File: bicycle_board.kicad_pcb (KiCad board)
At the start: 2 copper layers, 41.4 x 84.9 mm, 130 parts, among them J1 Micro_SD_Card, J10 USB_A, J12 Conn_01x04, J13 Conn_01x04, J2 USB_C_Receptacle_USB2.0_16P, J3 Conn_01x02, J4 Conn_01x02, J6 Conn_01x08, J7 Conn_01x05, J8 Conn_01x02, J9 Conn_01x06, Q1 Q_NMOS_GSD, Q2 Q_NMOS_GSD, Q3 Q_NMOS_GSD, Q4 Q_NMOS_GSD, Q5 Q_NMOS_GSD, Q6 Si2302, Q7 Si2302, Q8 Q_PMOS_GSD, U1 TP4056, U10 MCP603-xCH, U11 BMP280, U12 MMC5633NJL, U13 NS4168, U14 ESP32-C3-WROOM-02U, U15 CH32V203C8T6, U16 PS7516, U17 TXB0108PW, U2 SGM2039, U3 IIM-42652, U4 QMI8610, U5 AHT20, U6 SGM2033-1.8, U7 74HC595, U8 74HC595, U9 PCA9306DC1, Y1 12MHz, Y2 32.768kHz

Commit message: 连接大多数布线，做一些调整，添加覆铜
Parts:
- added C48: 100n, Capacitor_SMD:C_0402_1005Metric, B.Cu at (131.8, 106.5)
- J12: moved to F.Cu
- moved R26 16.2 mm to (133.9, 126.9), turned to -90 degrees
- moved R25 15.5 mm to (132.9, 126.9), turned to -90 degrees
- moved U9 11.5 mm to (132.5, 130.2), turned to 90 degrees
- moved R24 10.4 mm to (134.0, 133.4), turned to 90 degrees
- moved C18 9.34 mm to (130.7, 130.6), turned to 90 degrees
- moved R23 9.18 mm to (133.0, 133.4), turned to 90 degrees
- moved C11 8.68 mm to (118.2, 130.6)
- moved U4 8.68 mm to (120.5, 130.6)
- moved U3 8.68 mm to (124.8, 130.3)
- moved C10 8.68 mm to (124.0, 132.5)
- moved C12 8.68 mm to (121.0, 132.3)
- moved C33 8.68 mm to (127.5, 132.0)
- moved C9 8.68 mm to (125.8, 132.5)
- moved C17 7.51 mm to (131.5, 133.2), turned to 0 degrees
- moved C19 2.52 mm to (130.7, 138.5), turned to 0 degrees
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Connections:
- J12 pad 1: unconnected-(J12-Pin_1-Pad1) -> +3.3V
- J12 pad 2: /SCL2 -> GND
- J12 pad 3: /SDA2 -> /SCL2
- J12 pad 4: unconnected-(J12-Pin_4-Pad4) -> /SDA2
- U11 pad 2: /sensors/SPISen_CS_BMP_1V8 -> +1V8
- U11 pad 3: /sensors/SPISen_MOSI_1V8 -> /sensors/SDA1V8
- U11 pad 4: /sensors/SPISen_SCLK_1V8 -> /sensors/SCL1V8
- U11 pad 5: /sensors/SPISen_MISO_1V8 -> unconnected-(U11-SDO-Pad5)
- U13 pad 4: /I2SO_SDATA -> /I2SO_SD
- U14 pad 10: /I2SO_SD -> unconnected-(U14-IO10-Pad10)
- U14 pad 15: /I2SI_SD -> unconnected-(U14-IO3-Pad15)
- U14 pad 3: /I2SI_BCK -> unconnected-(U14-IO4-Pad3)
- U14 pad 4: /I2SI_WS -> /I2SO_SD
- U14 pad 7: /I2SO_WS -> /I2SO_BCK
- U14 pad 8: /I2SO_BCK -> /I2SO_WS
- U15 pad 16: unconnected-(U15-PA6-Pad16) -> /ADC_Isolar
- U15 pad 17: unconnected-(U15-PA7-Pad17) -> /ADC_Vbat
- U15 pad 18: unconnected-(U15-PB0-Pad18) -> /ADC_Vsolar
- U15 pad 21: /TXD -> /SCL2
- U15 pad 22: unconnected-(U15-PB11-Pad22) -> /SDA2
- U15 pad 26: unconnected-(U15-PB13-Pad26) -> /SPI_SCLK
- U15 pad 27: unconnected-(U15-PB14-Pad27) -> /SPI_MISO
- U15 pad 28: unconnected-(U15-PB15-Pad28) -> /SPI_MOSI
- U15 pad 30: unconnected-(U15-PA9-Pad30) -> /TXD
- U15 pad 31: unconnected-(U15-PA10-Pad31) -> /RXD
- U15 pad 32: unconnected-(U15-PA11-Pad32) -> /USB_CH32FS_D-
- U15 pad 33: unconnected-(U15-PA12-Pad33) -> /USB_CH32FS_D+
- U15 pad 38: unconnected-(U15-PA15-Pad38) -> /SPISen_CS_QMI_3V3
- U15 pad 39: unconnected-(U15-PB3-Pad39) -> /SPISen_SCLK_3V3
- U15 pad 40: unconnected-(U15-PB4-Pad40) -> /SPISen_MISO_3V3
- U15 pad 41: unconnected-(U15-PB5-Pad41) -> /SPISen_MOSI_3V3
- U15 pad 42: /USB_CH32FS_D- -> /SPISen_CS_TDK_3V3
- U15 pad 43: /USB_CH32FS_D+ -> /TDK_INT2_3V3
- U15 pad 45: unconnected-(U15-PB8-Pad45) -> /SCL1
- U15 pad 46: /RXD -> /SDA1
- U15 pad 7: unconnected-(U15-NRST-Pad7) -> Net-(U15-NRST)
- U17 pad 1: /sensors/SPISen_CS_QMI_1V8 -> unconnected-(U17-A1-Pad1)
- U17 pad 12: unconnected-(U17-B8-Pad12) -> /TDK_INT2_3V3
- U17 pad 13: /sensors/TDK_INT2_3V3 -> /SPISen_CS_TDK_3V3
- U17 pad 14: /sensors/SPISen_MISO_3V3 -> /SPISen_MOSI_3V3
- U17 pad 15: /sensors/SPISen_SCLK_3V3 -> /SPISen_MISO_3V3
- U17 pad 16: /sensors/SPISen_MOSI_3V3 -> /SPISen_SCLK_3V3
- U17 pad 17: /sensors/SPISen_CS_BMP_3V3 -> /SPISen_CS_QMI_3V3
- U17 pad 18: /sensors/SPISen_CS_TDK_3V3 -> unconnected-(U17-B2-Pad18)
- U17 pad 20: /sensors/SPISen_CS_QMI_3V3 -> unconnected-(U17-B1-Pad20)
- U17 pad 3: /sensors/SPISen_CS_TDK_1V8 -> unconnected-(U17-A2-Pad3)
- U17 pad 4: /sensors/SPISen_CS_BMP_1V8 -> /sensors/SPISen_CS_QMI_1V8
- U17 pad 5: /sensors/SPISen_MOSI_1V8 -> /sensors/SPISen_SCLK_1V8
- U17 pad 6: /sensors/SPISen_SCLK_1V8 -> /sensors/SPISen_MISO_1V8
- U17 pad 7: /sensors/SPISen_MISO_1V8 -> /sensors/SPISen_MOSI_1V8
- U17 pad 8: /sensors/TDK_INT2_1V8 -> /sensors/SPISen_CS_TDK_1V8
- U17 pad 9: unconnected-(U17-A8-Pad9) -> /sensors/TDK_INT2_1V8
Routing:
- net +3.3V: track 37.0 -> 362.9 mm, vias 1 -> 9
- net +BATT: track 55.2 -> 176.3 mm, vias 5 -> 6
- net GND: track 137.2 -> 218.7 mm, vias 9 -> 22
- net /SPI_MISO: track 29.5 -> 74.6 mm, vias 1 -> 2
- net /TXD: track 0.00 -> 43.0 mm, vias 0 -> 2
- net /SPK_EN: track 0.00 -> 42.2 mm, vias 0 -> 1
- net /RXD: track 0.00 -> 40.6 mm, vias 0 -> 2
- net +1V8: track 23.5 -> 64.0 mm, vias 1 -> 4
- net /SPI_MOSI: track 31.7 -> 70.6 mm, vias 3 -> 4
- net /USB_ESP_D+: track 3.31 -> 41.8 mm
- net /SPI_SCLK: track 44.7 -> 82.7 mm, vias 3 -> 4
- net /USB_ESP_D-: track 3.15 -> 40.4 mm
- net /ADC_Vbat: track 2.18 -> 34.1 mm, vias 0 -> 2
- net /ADC_Isolar: track 4.04 -> 35.3 mm, vias 0 -> 1
- net /SCL1: track 1.40 -> 31.8 mm, vias 0 -> 3
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- added copper zone on F.Cu, net +3.3V
- added copper zone on B.Cu, net GND
- added copper zone on F.Cu, net GND

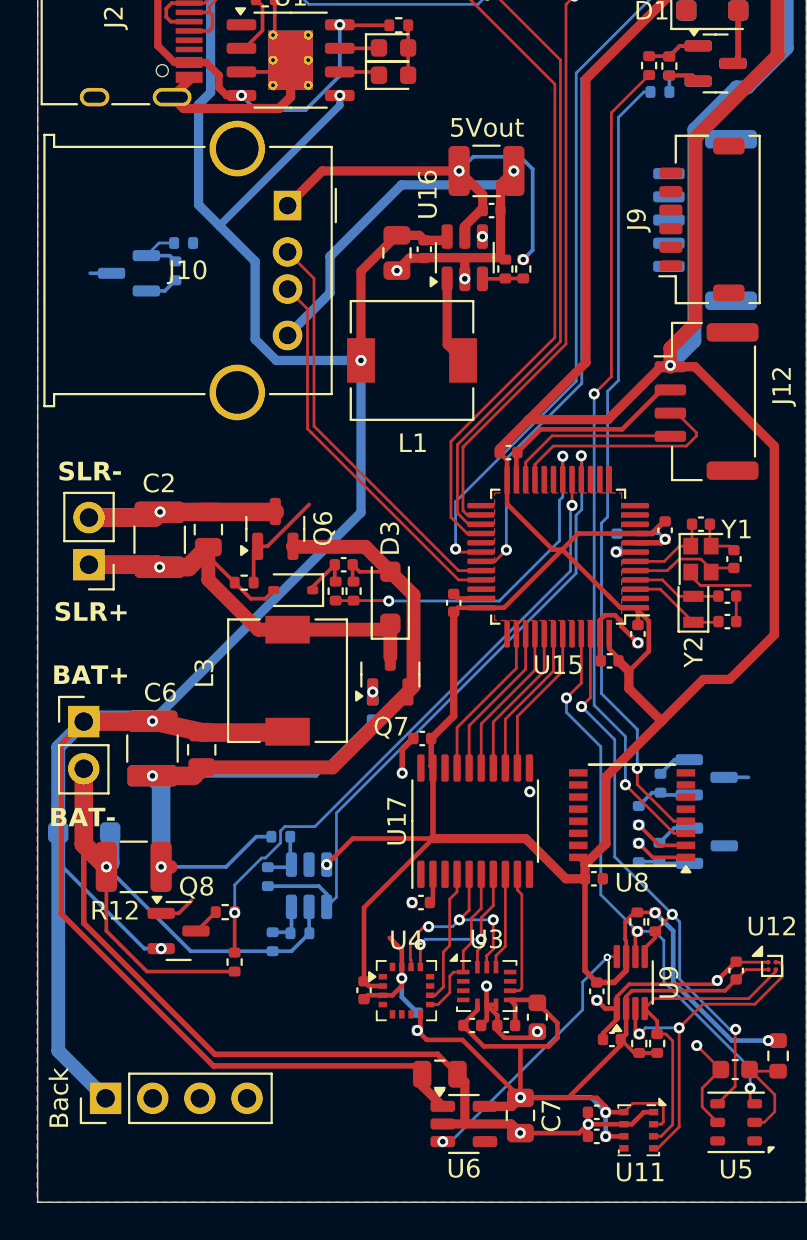
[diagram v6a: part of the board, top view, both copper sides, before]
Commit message: 移除第二个74HC595，SGM2033-1.8改成一直开启，按PCA9306数据手册修改供电
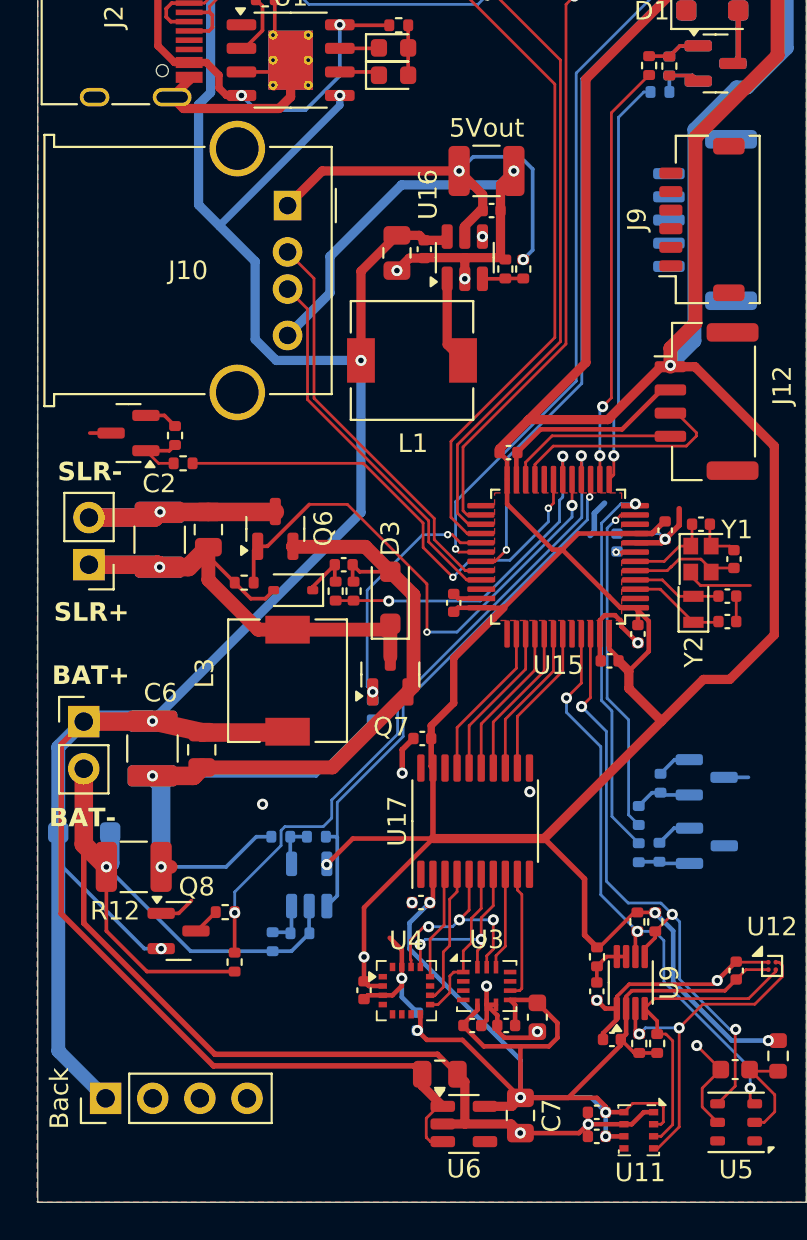
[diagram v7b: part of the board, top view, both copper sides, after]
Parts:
- removed C43: 100nF, Capacitor_SMD:C_0402_1005Metric
- removed U10: MCP603-xCH, Package_TO_SOT_SMD:SOT-23-6
- added R35: 200k, Resistor_SMD:R_0402_1005Metric, F.Cu at (130.7, 128.8)
- Q1, R1, R2: moved to F.Cu
- U8: value 74HC595 -> SGM8040-1; footprint Package_SO:SSOP-16_4.4x5.2mm_P0.65mm -> Package_TO_SOT_SMD:SOT-23-5; moved to B.Cu
- moved U8 17.8 mm to (115.2, 124.9), turned to 90 degrees
- moved R2 11.9 mm to (108.4, 102.2)
- moved R1 8.88 mm to (108.0, 100.7), turned to 90 degrees
- moved Q1 8.61 mm to (105.5, 100.5)
- moved R20 3.39 mm to (115.6, 122.3), turned to 0 degrees
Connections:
- C18 pad 2: +3.3V -> Net-(U9-EN)
- Q7 pad 1: /power/PWM_solarL -> /PWM_solarL
- R18 pad 2: Net-(U10-+) -> Net-(U8-+)
- R19 pad 2: Net-(U10--) -> Net-(U8--)
- R20 pad 1: Net-(U10--) -> Net-(U8--)
- R21 pad 2: Net-(U10-+) -> Net-(U8-+)
- R29 pad 1: /power/PWM_solarL -> /PWM_solarL
- U15 pad 11: unconnected-(U15-PA1-Pad11) -> /CH3
- U15 pad 12: unconnected-(U15-PA2-Pad12) -> /CH2
- U15 pad 13: unconnected-(U15-PA3-Pad13) -> /CH5
- U15 pad 14: unconnected-(U15-PA4-Pad14) -> /CH4
- U15 pad 15: unconnected-(U15-PA5-Pad15) -> /ADC_Isolar
- U15 pad 16: /ADC_Isolar -> /ADC_Vbat
- U15 pad 17: /ADC_Vbat -> /PWM_solar
- U15 pad 19: unconnected-(U15-PB1-Pad19) -> /CH1
- U15 pad 29: unconnected-(U15-PA8-Pad29) -> /PWM_solarL
- U17 pad 18: unconnected-(U17-B2-Pad18) -> /sensors/QMI_INT1_3V3
- U17 pad 3: unconnected-(U17-A2-Pad3) -> /sensors/QMI_INT1
- U6 pad 3: /SenEN -> +BATT
- U8 pad 1: /CH2 -> /ADC_Isolar
- U8 pad 2: /CH3 -> GND
- U8 pad 3: /CH4 -> Net-(U8-+)
- U8 pad 4: /CH5 -> Net-(U8--)
- U8 pad 5: /SenEN -> +3.3V
- U9 pad 7: +3.3V -> Net-(U9-EN)
- U9 pad 8: /SenEN -> Net-(U9-EN)
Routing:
- net /CH1: track 0.00 -> 26.1 mm, vias 0 -> 2
- net /PWM_solar: track 5.76 -> 28.9 mm, vias 0 -> 2
- net /CH4: track 44.5 -> 22.9 mm
- net /CH5: track 42.9 -> 22.0 mm
- net /CH2: track 2.86 -> 20.4 mm
- net /CH3: track 3.00 -> 18.5 mm
- net /SenEN: track 14.4 -> 0.00 mm, vias 2 -> 0
- net /PWM_solarL: track 0.00 -> 13.6 mm, vias 0 -> 2
- net +1V8: track 64.0 -> 77.4 mm, vias 4 -> 5
- net /sensors/QMI_INT1: track 0.00 -> 5.85 mm
- net /ADC_Isolar: track 35.3 -> 29.5 mm
- net +3.3V: track 362.9 -> 357.4 mm, vias 9 -> 10
- net GND: track 218.7 -> 222.7 mm, vias 22 -> 23
- net +BATT: track 176.3 -> 179.4 mm
- net /ADC_Vbat: track 34.1 -> 37.0 mm
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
